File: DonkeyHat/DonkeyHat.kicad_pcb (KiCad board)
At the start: 2 copper layers, 65 x 56.1 mm, 16 parts, among them J1 GPIO, J2 Encoder 2, J3 Encoder 1, U2 rp2040-zero

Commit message: New PCB
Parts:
- removed MH1, MH2, MH3, MH4: MountingHole_2.7mm_M2.5, MountingHole:MountingHole_2.7mm_M2.5
- added J4: B4B-PH-K-S_LF__SN_, Connector_JST:JST_SH_BM04B-SRSS-TB_1x04-1MP_P1.00mm_Vertical, F.Cu at (118.2, 78.1)
- renumbered OLED1 to OLED
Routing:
- net GND: track 95.8 -> 0.00 mm, vias 0 -> 1
- net Enc1A: track 76.7 -> 0.00 mm
- net +3V3: track 66.4 -> 0.00 mm, vias 1 -> 0
- net /GPIO2/SDA1: track 60.5 -> 0.00 mm
- net /GPIO3/SCL1: track 58.3 -> 0.00 mm
- net Net-(St1-Pin_1): track 52.8 -> 0.00 mm
- net +5V: track 51.7 -> 0.00 mm
- net Enc1B: track 50.4 -> 0.00 mm, vias 2 -> 0
- net Enc2B: track 48.6 -> 0.00 mm, vias 2 -> 0
- net Net-(In2-Pin_1): track 47.6 -> 0.00 mm, vias 1 -> 0
- net Enc2A: track 47.0 -> 0.00 mm, vias 2 -> 0
- net Net-(Thr1-Pin_1): track 38.5 -> 0.00 mm, vias 1 -> 0
- net /GPIO14/TXD0: track 24.0 -> 0.00 mm
- net /GPIO15/RXD0: track 20.4 -> 0.00 mm
- net +BATT: track 15.5 -> 0.00 mm
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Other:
- board size 65 x 56.1 mm -> 65 x 56.2 mm
- board text added: "- +"
- board text added: "5V"
- board text added: "Donkeyhat V1.0"
- board text added: "I2C"
- board text removed: "-"
- board text removed: "- 5V +"
- board text removed: "Donkeyhat V0.2"
- board text removed: "I2C - + SCL SDA"
- board text removed: "PoE"
- board text removed: "RJ45"
- board text removed: "USB"

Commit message: WIP
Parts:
- removed In1: RC 1, Connector_PinHeader_2.54mm:PinHeader_1x03_P2.54mm_Vertical
- removed In2, In3, St1, Thr1: Conn_01x03_Pin, Connector_PinHeader_2.54mm:PinHeader_1x03_P2.54mm_Vertical
- removed OLED: Conn_01x04_Pin, Connector_PinHeader_2.54mm:PinHeader_1x04_P2.54mm_Vertical
- added J5: Conn_02x03_Odd_Even, Connector_PinHeader_2.54mm:PinHeader_2x03_P2.54mm_Vertical, F.Cu at (103.4, 84.9)
- added J6: Conn_02x03_Odd_Even, Connector_PinHeader_2.54mm:PinHeader_2x03_P2.54mm_Vertical, F.Cu at (103.3, 77.2)
- added OLED1: Conn_01x04_Pin, Connector_PinHeader_2.54mm:PinHeader_1x04_P2.54mm_Vertical, F.Cu at (128.1, 70.9)
- added Throttle1: Conn_01x03_Pin, Connector_PinHeader_2.54mm:PinHeader_1x03_P2.54mm_Vertical, F.Cu at (103.3, 79.8)
- J4: value B4B-PH-K-S_LF__SN_ -> I2C
- moved J3 0.86 mm to (109.4, 94.8)
- moved J2 0.29 mm to (109.4, 97.4)
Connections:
- J1 pad 10: /GPIO15/RXD0 -> unconnected-(J1-Pin_10-Pad10)
- U2 pad 1: /GPIO15/RXD0 -> unconnected-(U2-0-Pad1)
- U2 pad 11: Net-(St1-Pin_1) -> Throttle
- U2 pad 12: Net-(Thr1-Pin_1) -> Steer
- U2 pad 17: Net-(In2-Pin_1) -> RCin2
- U2 pad 18: Net-(In3-Pin_1) -> RCin1
- U2 pad 2: /GPIO14/TXD0 -> unconnected-(U2-1-Pad2)
- U2 pad 20: Net-(In1-Pin_1) -> RCin3
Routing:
- net GND: vias 1 -> 0
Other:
- outline, holes or cut-outs redrawn
- board text added: "2"
- board text added: "3"
- board text added: "Ch1"
- board text added: "Str"
- board text added: "Thr"
- board text added: "|"
- board text removed: "In1"
- board text removed: "In2"
- board text removed: "In3"
- board text removed: "Steer"
- board text removed: "Throt"

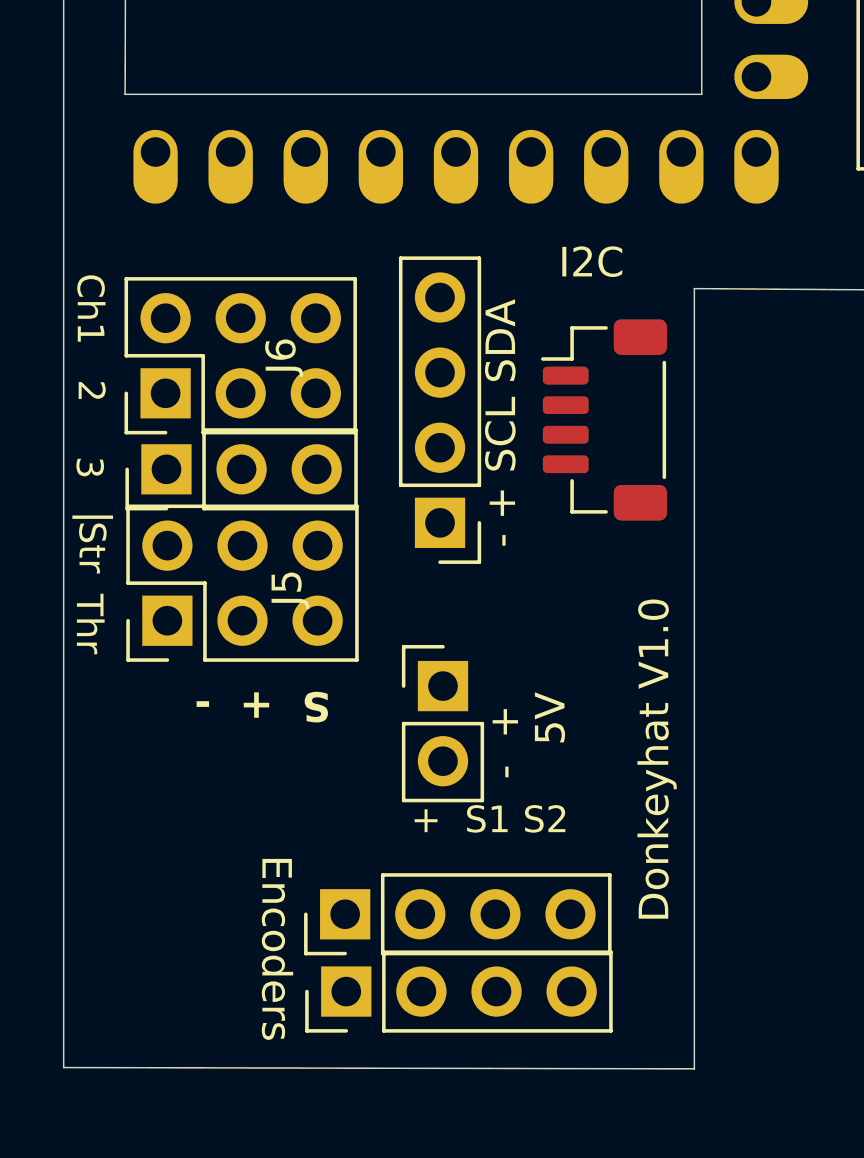
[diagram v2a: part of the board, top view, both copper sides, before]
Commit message: UI improvements
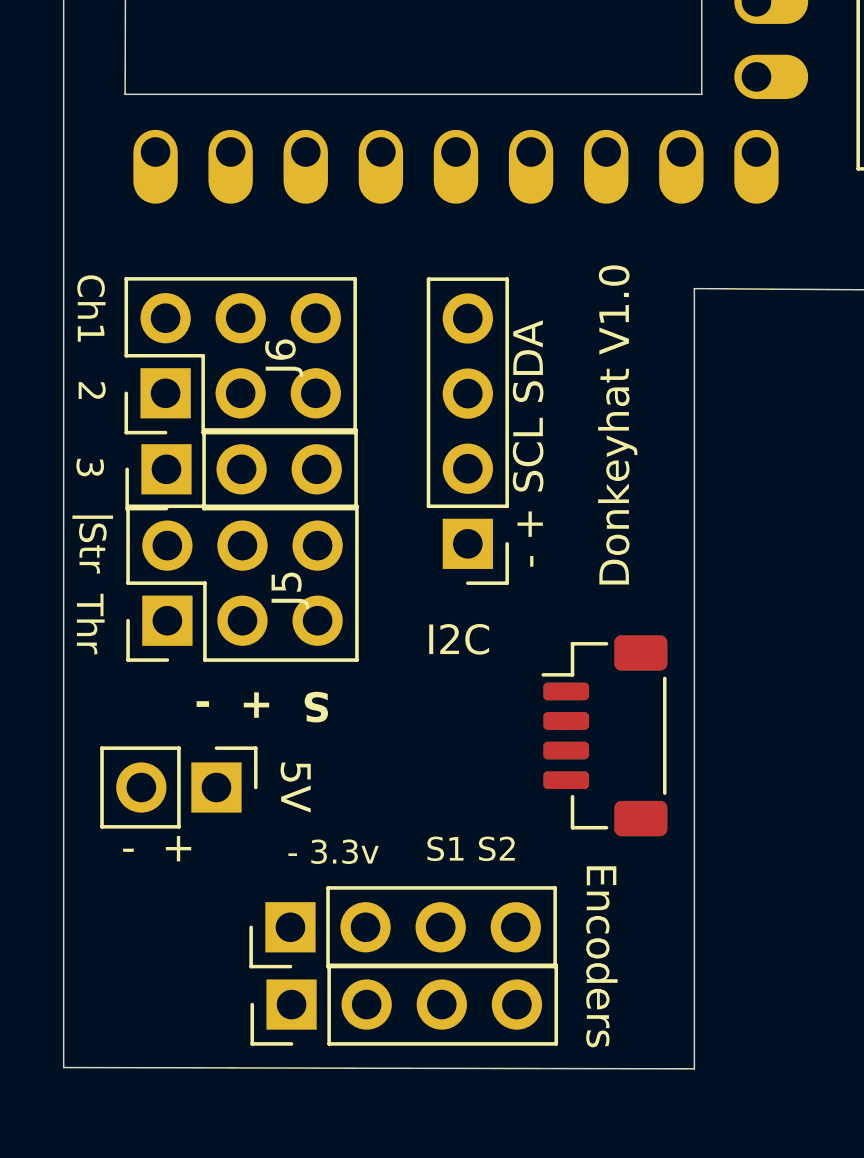
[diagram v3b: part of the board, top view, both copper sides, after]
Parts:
- moved J4 10.7 mm to (118.2, 88.8)
- moved 5V1 8.39 mm to (105.0, 90.5), turned to -90 degrees
- moved J2 1.90 mm to (107.6, 97.9)
- moved J3 1.90 mm to (107.5, 95.3)
- moved I2C1 1.18 mm to (113.5, 82.3)
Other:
- board text added: "- 3.3v"
- board text added: "S1 S2"
- board text removed: "+ S1 S2"

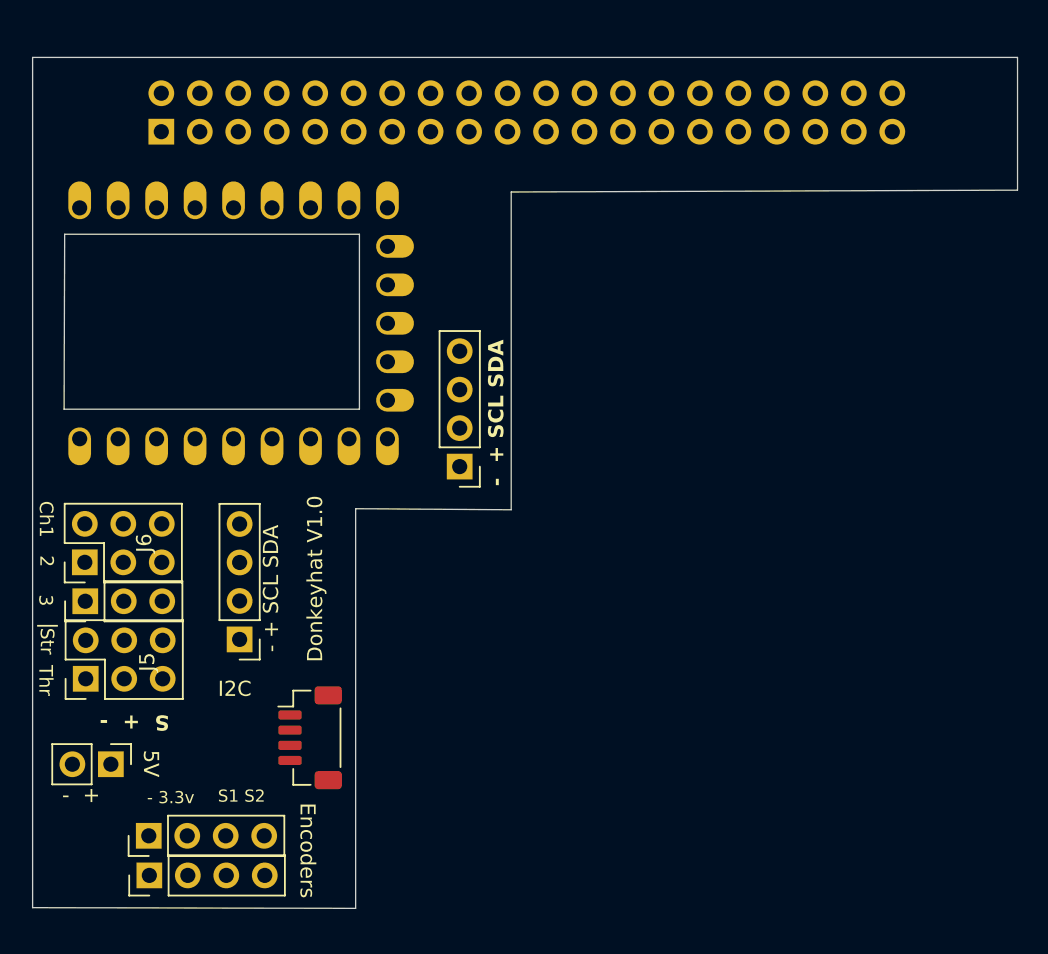
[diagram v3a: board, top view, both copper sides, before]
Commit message: Battery power for servos
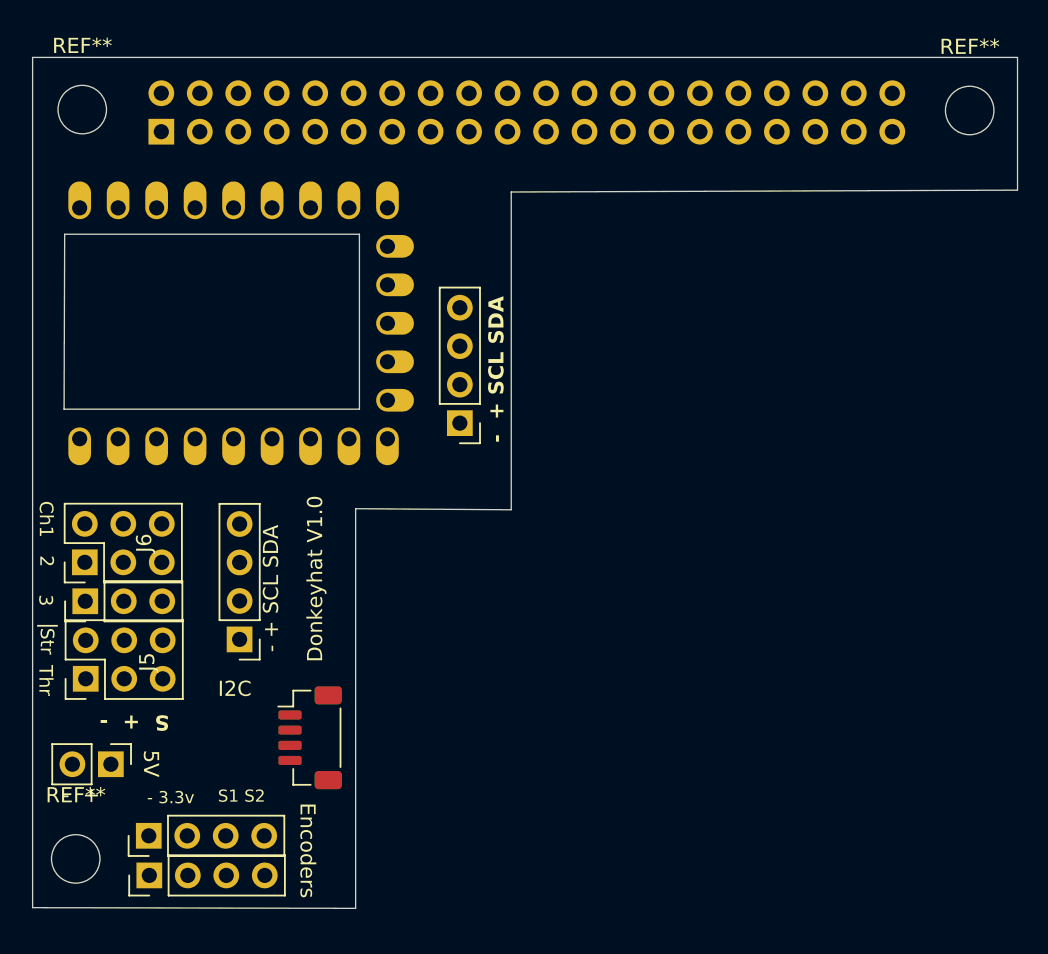
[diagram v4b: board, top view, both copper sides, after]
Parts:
- added REF**: MountingHole_3.2mm_M3, MountingHole:MountingHole_3.2mm_M3, F.Cu at (102.7, 96.8)
- added REF**: MountingHole_3.2mm_M3, MountingHole:MountingHole_3.2mm_M3, F.Cu at (103.2, 47.3)
- added REF**: MountingHole_3.2mm_M3, MountingHole:MountingHole_3.2mm_M3, F.Cu at (161.7, 47.4)
- moved OLED1 2.87 mm to (128.1, 68.0)
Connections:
- J1 pad 10: unconnected-(J1-Pin_10-Pad10) -> Rpi Rx
- J1 pad 8: /GPIO14/TXD0 -> Rpi Tx
- J5 pad 3: +5V -> Batt
- J5 pad 4: +5V -> Batt
- U2 pad 1: unconnected-(U2-0-Pad1) -> Rpi Rx
- U2 pad 2: unconnected-(U2-1-Pad2) -> Rpi Tx
